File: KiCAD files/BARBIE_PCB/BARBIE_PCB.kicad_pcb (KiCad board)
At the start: 2 copper layers, 104.9 x 42.4 mm, 10 parts, among them J1 Conn_01x14_Pin, J2 Conn_01x12_Pin, J3 Conn_01x08_Pin, J4 Conn_01x14_Pin, J5 Conn_01x08_Pin, J6 Conn_01x12_Pin, J7 Conn_01x12_Pin, U1 ESP32-S3-WROOM-1U-N8, U2 LORA-CC68-433MHz-TCXO, U3 ATGM332D-5N71

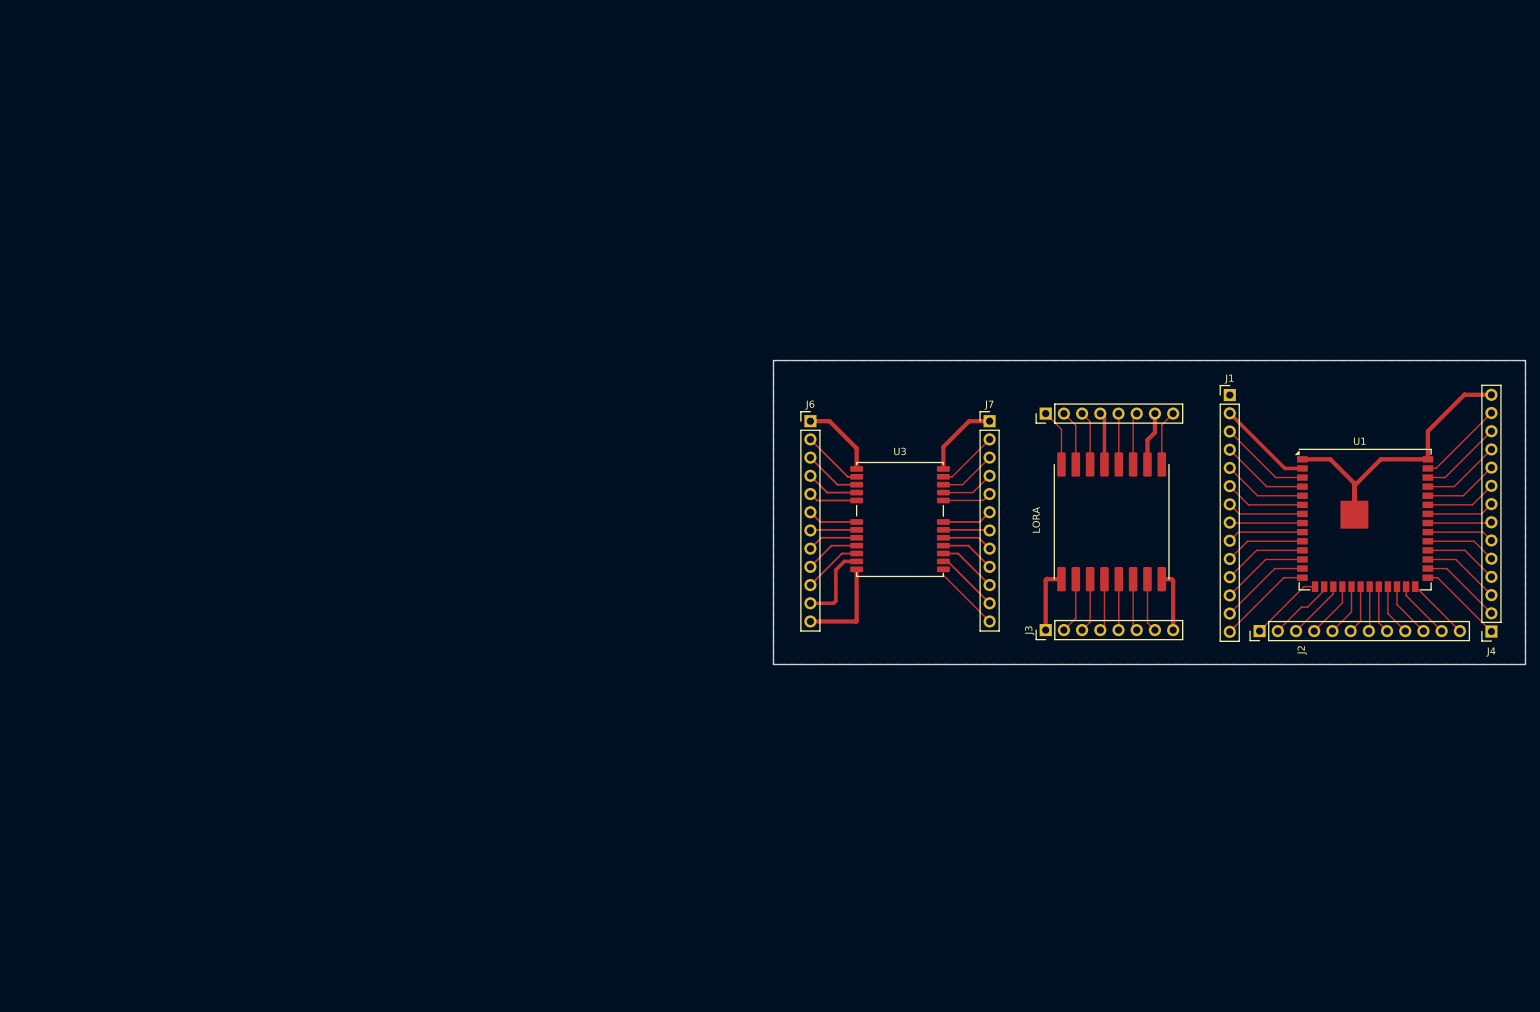
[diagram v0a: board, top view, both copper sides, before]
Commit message: Integrated Hannah's schematic into the main schematic
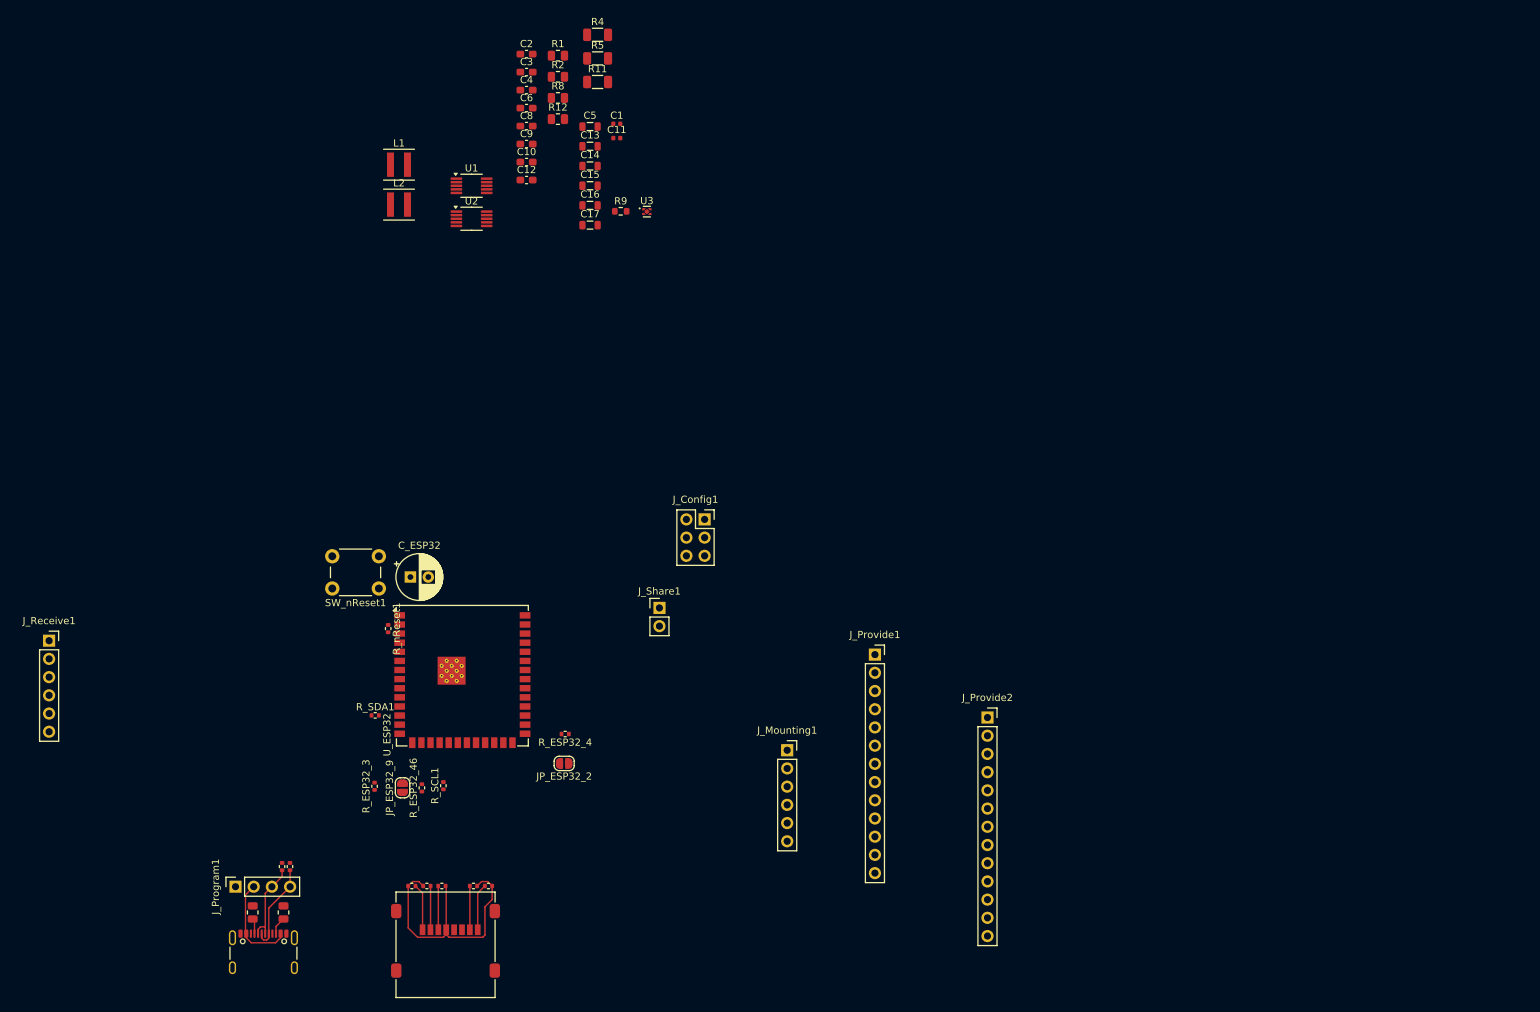
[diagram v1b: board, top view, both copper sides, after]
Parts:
- removed J1: Conn_01x14_Pin, Connector_PinHeader_2.54mm:PinHeader_1x14_P2.54mm_Vertical
- removed J2, J6, J7: Conn_01x12_Pin, Connector_PinHeader_2.54mm:PinHeader_1x12_P2.54mm_Vertical
- removed J3, J5: Conn_01x08_Pin, Connector_PinHeader_2.54mm:PinHeader_1x08_P2.54mm_Vertical
- removed J4: Conn_01x14_Pin, Connector_PinSocket_2.54mm:PinSocket_1x14_P2.54mm_Vertical
- added C1: 100nF, Inductor_SMD:L_0402_1005Metric, F.Cu at (103.9, 69.0)
- added C10: 10uF, Capacitor_SMD:C_0603_1608Metric_Pad1.08x0.95mm_HandSolder, F.Cu at (91.3, 74.3)
- added C11: 100nF, Inductor_SMD:L_0402_1005Metric, F.Cu at (103.9, 71.0)
- added C12: 10uF, Capacitor_SMD:C_0603_1608Metric_Pad1.08x0.95mm_HandSolder, F.Cu at (91.3, 76.8)
- added C13: 22uF, Inductor_SMD:L_0805_2012Metric, F.Cu at (100.2, 72.1)
- added C14: 22uF, Inductor_SMD:L_0805_2012Metric, F.Cu at (100.2, 74.9)
- added C15: 22uF, Inductor_SMD:L_0805_2012Metric, F.Cu at (100.2, 77.6)
- added C16: 22uF, Inductor_SMD:L_0805_2012Metric, F.Cu at (100.2, 80.4)
- added C17: 22uF, Inductor_SMD:L_0805_2012Metric, F.Cu at (100.2, 83.1)
- added C2: 10uF, Capacitor_SMD:C_0603_1608Metric_Pad1.08x0.95mm_HandSolder, F.Cu at (91.3, 59.2)
- added C3: 10uF, Capacitor_SMD:C_0603_1608Metric_Pad1.08x0.95mm_HandSolder, F.Cu at (91.3, 61.8)
- added C4: 10uF, Capacitor_SMD:C_0603_1608Metric_Pad1.08x0.95mm_HandSolder, F.Cu at (91.3, 64.3)
- added C5: 22uF, Inductor_SMD:L_0805_2012Metric, F.Cu at (100.2, 69.4)
- added C6: 10uF, Capacitor_SMD:C_0603_1608Metric_Pad1.08x0.95mm_HandSolder, F.Cu at (91.3, 66.8)
- added C8: 10uF, Capacitor_SMD:C_0603_1608Metric_Pad1.08x0.95mm_HandSolder, F.Cu at (91.3, 69.3)
- added C9: 10uF, Capacitor_SMD:C_0603_1608Metric_Pad1.08x0.95mm_HandSolder, F.Cu at (91.3, 71.8)
- added C_ESP32: C_Polarized_US, Capacitor_THT:CP_Radial_D6.3mm_P2.50mm, F.Cu at (75.1, 132.2)
- added JP_ESP32_2: SolderJumper_2_Open, Jumper:SolderJumper-2_P1.3mm_Open_RoundedPad1.0x1.5mm, F.Cu at (96.5, 158.2)
- added JP_ESP32_9: SolderJumper_2_Open, Jumper:SolderJumper-2_P1.3mm_Open_RoundedPad1.0x1.5mm, F.Cu at (74.0, 161.6)
- added J_Config1: Conn_02x03_Odd_Even, Connector_PinSocket_2.54mm:PinSocket_2x03_P2.54mm_Vertical, F.Cu at (116.1, 124.2)
- added J_Mounting1: Conn_01x06_Pin, Connector_PinSocket_2.54mm:PinSocket_1x06_P2.54mm_Vertical, F.Cu at (127.7, 156.4)
- added J_Program1: Conn_01x04_Socket, Connector_PinSocket_2.54mm:PinSocket_1x04_P2.54mm_Vertical, F.Cu at (50.7, 175.4)
- added J_Provide1: Conn_01x13, Connector_PinSocket_2.54mm:PinSocket_1x13_P2.54mm_Vertical, F.Cu at (139.9, 143.0)
- added J_Provide2: Conn_01x13, Connector_PinSocket_2.54mm:PinSocket_1x13_P2.54mm_Vertical, F.Cu at (155.6, 151.8)
- added J_Receive1: Conn_01x06_Pin, Connector_PinSocket_2.54mm:PinSocket_1x06_P2.54mm_Vertical, F.Cu at (24.7, 141.1)
- added J_SD_Card1: Micro_SD_Card, Connector_Card:microSD_HC_Molex_47219-2001, F.Cu at (80.0, 183.5)
- added J_Share1: Conn_01x02_Pin, Connector_PinHeader_2.54mm:PinHeader_1x02_P2.54mm_Vertical, F.Cu at (109.8, 136.5)
- added J_USB_C1: USB_C_Receptacle_USB2.0_16P, Connector_USB:USB_C_Receptacle_GCT_USB4105-xx-A_16P_TopMnt_Horizontal, F.Cu at (54.6, 185.6)
- added L1: 1.5uH, Inductor_SMD:L_Coilcraft_XxL4020, F.Cu at (73.5, 74.7)
- added L2: 1.5uH, Inductor_SMD:L_Coilcraft_XxL4020, F.Cu at (73.5, 80.2)
- added R1: 470k, Resistor_SMD:R_0805_2012Metric, F.Cu at (95.7, 59.5)
- added R11: 10k, Resistor_SMD:R_1206_3216Metric, F.Cu at (101.2, 63.1)
- added R12: 220k, Resistor_SMD:R_0805_2012Metric, F.Cu at (95.7, 68.3)
- added R2: 150k, Resistor_SMD:R_0805_2012Metric, F.Cu at (95.7, 62.4)
- added R4: 10k, Resistor_SMD:R_1206_3216Metric, F.Cu at (101.2, 56.6)
- added R5: 10k, Resistor_SMD:R_1206_3216Metric, F.Cu at (101.2, 59.9)
- added R8: 470k, Resistor_SMD:R_0805_2012Metric, F.Cu at (95.7, 65.4)
- added R9: 120k, Resistor_SMD:R_0603_1608Metric, F.Cu at (104.4, 81.2)
- added R_CC1: 5.6kR, Resistor_SMD:R_0805_2012Metric, F.Cu at (53.1, 179.0)
- added R_CC2: 5.6kR, Resistor_SMD:R_0805_2012Metric, F.Cu at (57.4, 179.0)
- added R_D+1: 22R, Resistor_SMD:R_0402_1005Metric, F.Cu at (58.3, 172.6)
- added R_D-1: 22R, Resistor_SMD:R_0402_1005Metric, F.Cu at (57.2, 172.6)
- added R_ESP32_3: 1MR, Resistor_SMD:R_0402_1005Metric, F.Cu at (70.1, 161.4)
- added R_ESP32_4: 1MR, Resistor_SMD:R_0402_1005Metric, F.Cu at (96.7, 154.1)
- added R_ESP32_46: 1MR, Resistor_SMD:R_0402_1005Metric, F.Cu at (76.7, 161.6)
- added R_MISO1: 1MR, Resistor_SMD:R_0402_1005Metric, F.Cu at (83.9, 175.3)
- added R_MOSI1: 1MR, Resistor_SMD:R_0402_1005Metric, F.Cu at (79.5, 175.3)
- added R_SCL1: 1MR, Resistor_SMD:R_0402_1005Metric, F.Cu at (79.7, 161.3)
- added R_SDA1: 1MR, Resistor_SMD:R_0402_1005Metric, F.Cu at (70.2, 151.5)
- added R_SD_CARD1: 1MR, Resistor_SMD:R_0402_1005Metric, F.Cu at (86.0, 175.3)
- added R_SD_CARD2: 1MR, Resistor_SMD:R_0402_1005Metric, F.Cu at (75.3, 175.3)
- added R_SD_CARD_CS1: 1MR, Resistor_SMD:R_0402_1005Metric, F.Cu at (77.4, 175.3)
- added R_nReset1: 1MR, Resistor_SMD:R_0402_1005Metric, F.Cu at (72.0, 139.4)
- added SW_nReset1: SW_Push, Button_Switch_THT:SW_PUSH_6mm, F.Cu at (70.7, 133.8)
- added U_ESP32: ESP32-S3-WROOM-1, RF_Module:ESP32-S3-WROOM-1U, F.Cu at (82.3, 146.0)
- U1: value ESP32-S3-WROOM-1U-N8 -> TPS60701RNMR; footprint ESP32-WROOM-32UE_N4:ESP32-S3-WROOM-1U_No_holes -> Package_SO:MSOP-10_3x3mm_P0.5mm
- U2: value LORA-CC68-433MHz-TCXO -> TPS60701RNMR; footprint LORA-CC68-433MHz-TCXO:LORA-CC68-433MHz-TCXO -> Package_SO:MSOP-10_3x3mm_P0.5mm
- U3: value ATGM332D-5N71 -> TPS3831; footprint ATGM332D-5NR32:ATGM332D-5NR32 -> Package_SON:Texas_X2SON-4_1x1mm_P0.65mm
- moved U1 133.1 mm to (83.6, 77.6)
- moved U2 98.8 mm to (83.6, 82.2), turned to 0 degrees
- moved U3 55.6 mm to (108.1, 81.2)
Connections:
- U1 pad 1: GND -> Net-(U1-EN)
- U1 pad 10: /10 -> NEW_GND
- U1 pad 2: /2 -> Net-(U1-PG)
- U1 pad 3: /3 -> Net-(U1-VAUX)
- U1 pad 4: /4 -> NEW_GND
- U1 pad 5: /5 -> Net-(U1-FB)
- U1 pad 6: /6 -> NEW_GND
- U1 pad 7: /7 -> 3V3
- U1 pad 8: /8 -> 3V3
- U1 pad 9: /9 -> Net-(U1-L2)
- U2 pad 1: GND -> Net-(U2-EN)
- U2 pad 10: GND -> NEW_GND
- U2 pad 4: Net-(J3-Pin_4) -> NEW_GND
- U2 pad 6: Net-(J3-Pin_6) -> NEW_GND
- U2 pad 7: Net-(J3-Pin_7) -> 5V
- U2 pad 8: GND -> 5V
- U3 pad 1: Net-(J7-Pin_12) -> BATTERY_OK
- U3 pad 2: Net-(J7-Pin_11) -> unconnected-(U3-~{MR}-Pad2)
- U3 pad 3: Net-(J7-Pin_10) -> GND
- U3 pad 4: Net-(J7-Pin_9) -> V_BATTERY
- U3 pad 5: Net-(J7-Pin_8) -> unconnected-(U3-TP-Pad5)
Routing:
- net GND: track 106.5 -> 0.00 mm
- net +3V3: track 0.00 -> 36.8 mm
- net /USB_V: track 0.00 -> 13.6 mm
- net /2: track 13.3 -> 0.00 mm
- net /14: track 13.3 -> 0.00 mm
- net /3: track 12.8 -> 0.00 mm
- net /13: track 12.7 -> 0.00 mm
- net /USB_D+: track 0.00 -> 12.5 mm
- net /4: track 12.3 -> 0.00 mm
- net /12: track 12.2 -> 0.00 mm
- net /39: track 12.1 -> 0.00 mm
- net /27: track 12.0 -> 0.00 mm
- net /5: track 11.7 -> 0.00 mm
- net /11: track 11.7 -> 0.00 mm
- net /USB_D-: track 0.00 -> 11.6 mm
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- removed copper zone on B.Cu, net GND
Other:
- board outline removed
